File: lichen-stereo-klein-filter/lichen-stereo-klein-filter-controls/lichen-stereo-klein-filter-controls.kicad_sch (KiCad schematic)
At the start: 39 parts, among them J1 Thonkiconn_Mono_Audio_Jack, J2 Thonkiconn_Mono_Audio_Jack, J3 Thonkiconn_Mono_Audio_Jack, J4 Thonkiconn_Mono_Audio_Jack, J5 Thonkiconn_Mono_Audio_Jack, J6 Thonkiconn_Mono_Audio_Jack, J7 Conn_02x07_Top_Bottom, U1 TL074

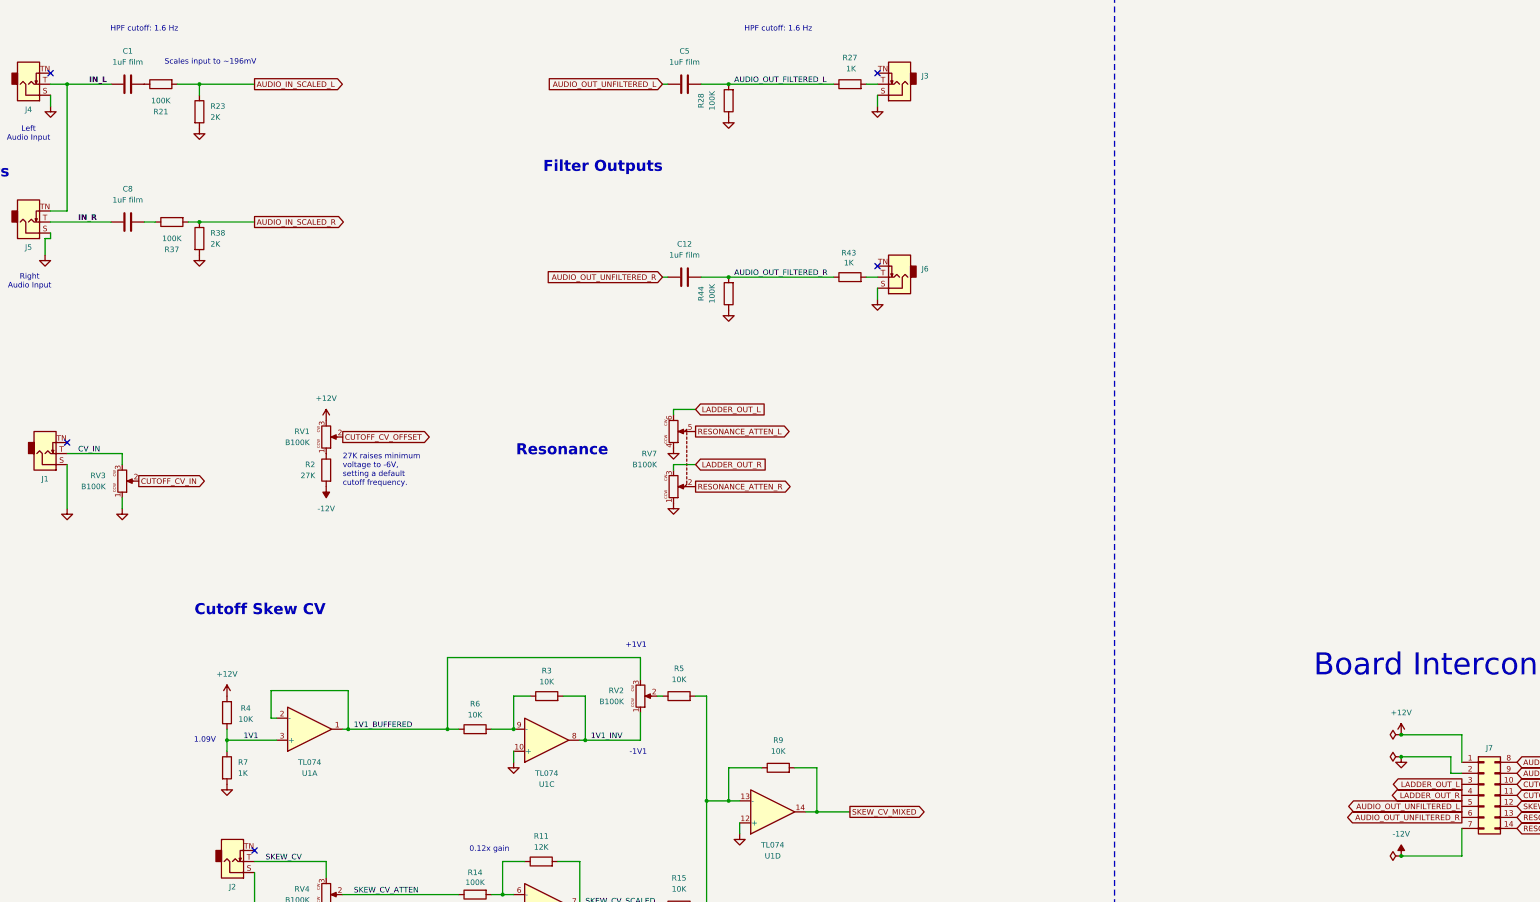
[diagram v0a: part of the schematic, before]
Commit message: feat: Updates Crustose, Cladonia and YouMe Transformer. Adds Stereo Latencies.
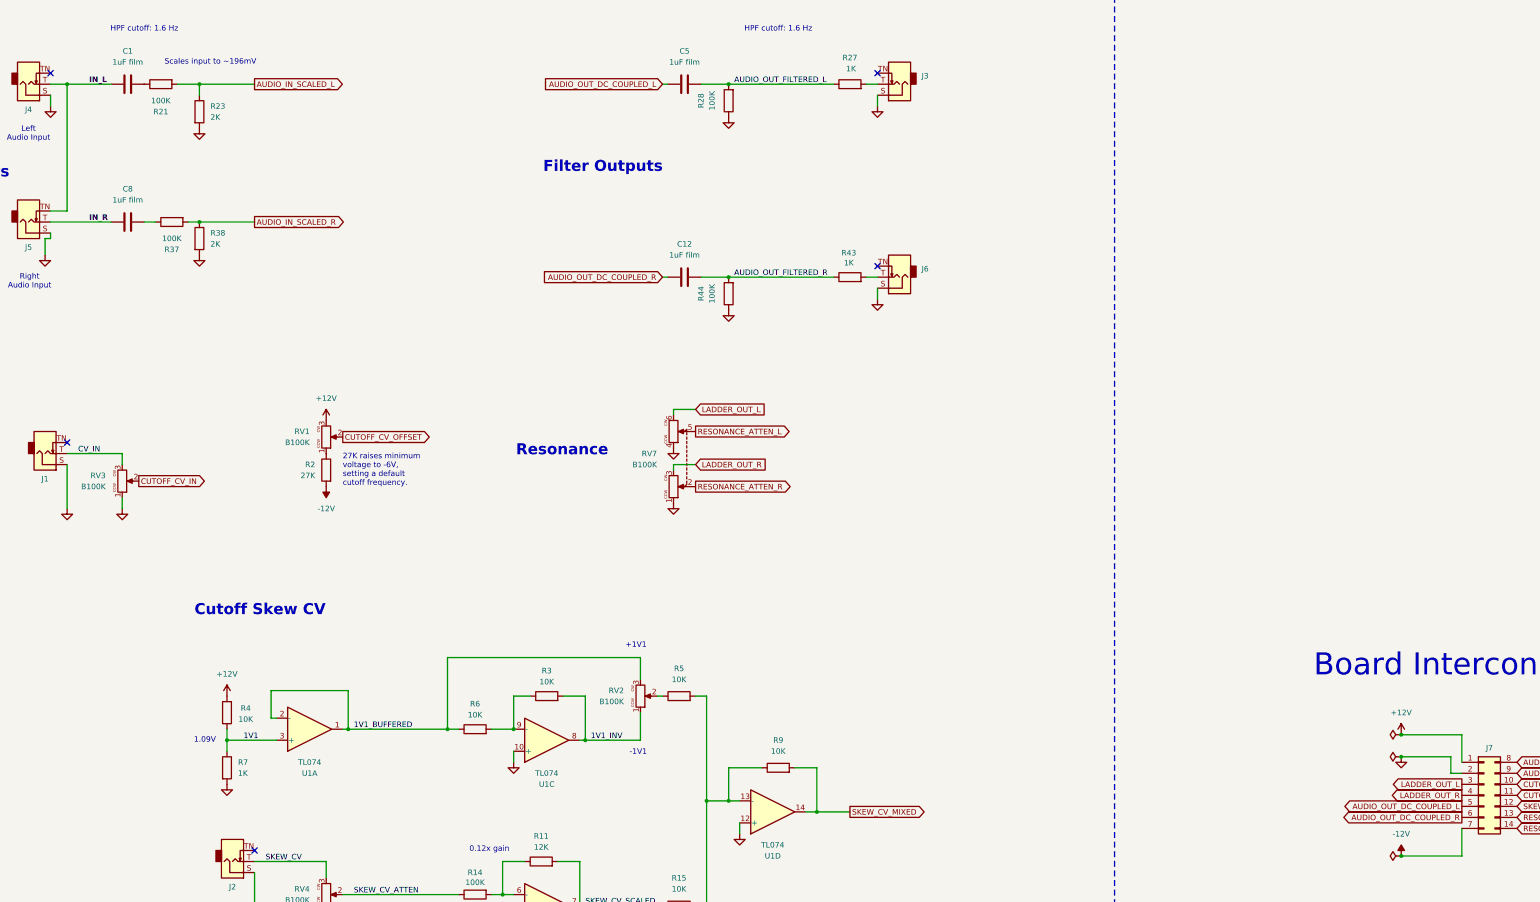
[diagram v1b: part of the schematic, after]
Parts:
- J3, J6: footprint Lichen:Audio_Jack_Thonkiconn_Mono -> Lichen:Audio_Jack_Thonkiconn_Mono_Right_Overhang
- J4, J5: footprint Lichen:Audio_Jack_Thonkiconn_Mono -> Lichen:Audio_Jack_Thonkiconn_Mono_Left_Overhang
- J7: value Conn_02x07_Top_Bottom -> 02x07 Socket; LCSC (none) -> C84005; Manufacturer (none) -> BOOMELE(Boom Precision Elec); Part Number (none) -> 2.54-2*7PFemale Headers
- R11: JLCPCB ID C22790 -> (none); LCSC (none) -> C22790
- R15, R3, R6, R9: JLCPCB ID C25804 -> (none); LCSC (none) -> C25804
- R4, R5: LCSC (none) -> C25804
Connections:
- net AUDIO_OUT_UNFILTERED_L renamed AUDIO_OUT_DC_COUPLED_L
- net AUDIO_OUT_UNFILTERED_R renamed AUDIO_OUT_DC_COUPLED_R
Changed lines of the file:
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@@
 	)
 	(label "IN_R"
-		(at 71.12 80.01 0)
+		(at 73.66 80.01 0)
 		(effects
 			(font
@@
 		)
 	)
-	(global_label "AUDIO_OUT_UNFILTERED_R"
+	(global_label "AUDIO_OUT_DC_COUPLED_R"
 		(shape output)
 		(at 389.89 217.17 180)
@@
 		)
 		(property "Intersheetrefs" "${INTERSHEET_REFS}"
-			(at 362.2909 217.17 0)
+			(at 361.3233 217.17 0)
 			(effects
 				(font
@@
 		)
 	)
-	(global_label "AUDIO_OUT_UNFILTERED_L"
+	(global_label "AUDIO_OUT_DC_COUPLED_L"
 		(shape output)
 		(at 389.89 214.63 180)
@@
 		)
 		(property "Intersheetrefs" "${INTERSHEET_REFS}"
-			(at 362.5328 214.63 0)
+			(at 361.5652 214.63 0)
 			(effects
 				(font
@@
 		)
 	)
-	(global_label "AUDIO_OUT_UNFILTERED_L"
+	(global_label "AUDIO_OUT_DC_COUPLED_L"
 		(shape input)
 		(at 205.74 48.26 180)
@@
 		)
 		(property "Intersheetrefs" "${INTERSHEET_REFS}"
-			(at 178.3828 48.26 0)
+			(at 177.4152 48.26 0)
 			(effects
 				(font
@@
 		)
 	)
-	(global_label "AUDIO_OUT_UNFILTERED_R"
+	(global_label "AUDIO_OUT_DC_COUPLED_R"
 		(shape input)
 		(at 205.74 92.71 180)
@@
 		)
 		(property "Intersheetrefs" "${INTERSHEET_REFS}"
-			(at 178.1409 92.71 0)
+			(at 177.1733 92.71 0)
 			(effects
 				(font
@@
 			)
 		)
-		(property "Datasheet" "https://jlcpcb.com/api/file/downloadByFileSystemAccessId/8579706381320323072"
+		(property "Datasheet" "https://www.lcsc.com/datasheet/lcsc_datasheet_2206010045_UNI-ROYAL-Uniroyal-Elec-0603WAF1002T5E_C25804.pdf"
 			(at 105.41 193.04 0)
 			(effects
@@
 			)
 		)
+		(property "LCSC" "C25804"
+			(at 104.14 177.8 0)
+			(effects
+				(font
+					(size 1.27 1.27)
+				)
+				(hide yes)
+			)
+		)
 		(pin "1"
 		)
@@
 			)
 		)
-		(property "Footprint" "Lichen:Audio_Jack_Thonkiconn_Mono"
+		(property "Footprint" "Lichen:Audio_Jack_Thonkiconn_Mono_Left_Overhang"
 			(at 60.706 32.512 0)
 			(effects
@@
 			)
 		)
-		(property "Footprint" "Lichen:Audio_Jack_Thonkiconn_Mono"
+		(property "Footprint" "Lichen:Audio_Jack_Thonkiconn_Mono_Right_Overhang"
 			(at 259.334 32.512 0)
 			(effects
@@
 		)
 		(instances
-			(project ""
+			(project "lichen-stereo-klein-filter-controls"
 				(path "/bf38fd3d-174f-4d81-a157-162ed62e96ed"
 					(reference "H2")
@@
 			)
 		)
-		(property "Datasheet" "https://jlcpcb.com/api/file/downloadByFileSystemAccessId/8579706381320323072"
+		(property "Datasheet" "https://www.lcsc.com/datasheet/lcsc_datasheet_2206010045_UNI-ROYAL-Uniroyal-Elec-0603WAF1002T5E_C25804.pdf"
 			(at 209.55 189.23 0)
 			(effects
@@
 			)
 		)
+		(property "LCSC" "C25804"
+			(at 224.79 187.96 0)
+			(effects
+				(font
+					(size 1.27 1.27)
+				)
+				(hide yes)
+			)
+		)
 		(pin "1"
 		)
@@
 		)
 		(instances
-			(project ""
+			(project "lichen-stereo-klein-filter-controls"
 				(path "/bf38fd3d-174f-4d81-a157-162ed62e96ed"
 					(reference "H1")
@@
 			)
 		)
-		(property "Datasheet" "https://jlcpcb.com/api/file/downloadByFileSystemAccessId/8579706381320323072"
+		(property "Datasheet" "https://www.lcsc.com/datasheet/lcsc_datasheet_2206010045_UNI-ROYAL-Uniroyal-Elec-0603WAF1002T5E_C25804.pdf"
 			(at 232.41 205.74 0)
 			(effects
@@
 			)
 		)
-		(property "JLCPCB ID" "C25804"
+		(property "LCSC" "C25804"
 			(at 247.65 204.47 0)
 			(effects
@@
 			)
 		)
-		(property "Footprint" "Lichen:Audio_Jack_Thonkiconn_Mono"
+		(property "Footprint" "Lichen:Audio_Jack_Thonkiconn_Mono_Right_Overhang"
 			(at 259.334 76.962 0)
 			(effects
@@
 			)
 		)
-		(property "Footprint" "Lichen:Audio_Jack_Thonkiconn_Mono"
+		(property "Footprint" "Lichen:Audio_Jack_Thonkiconn_Mono_Left_Overhang"
 			(at 60.706 64.262 0)
 			(effects
@@
 			)
 		)
-		(property "Datasheet" "https://jlcpcb.com/api/file/downloadByFileSystemAccessId/8579706381320323072"
+		(property "Datasheet" "https://www.lcsc.com/datasheet/lcsc_datasheet_2206010045_UNI-ROYAL-Uniroyal-Elec-0603WAF1002T5E_C25804.pdf"
 			(at 209.55 237.49 0)
 			(effects
@@
 			)
 		)
-		(property "JLCPCB ID" "C25804"
+		(property "LCSC" "C25804"
 			(at 224.79 236.22 0)
 			(effects
@@
 			)
 		)
-		(property "Datasheet" "https://jlcpcb.com/api/file/downloadByFileSystemAccessId/8579706381320323072"
+		(property "Datasheet" "https://www.lcsc.com/datasheet/lcsc_datasheet_2206010045_UNI-ROYAL-Uniroyal-Elec-0603WAF1002T5E_C25804.pdf"
 			(at 179.07 189.23 0)
 			(effects
@@
 			)
 		)
-		(property "JLCPCB ID" "C25804"
+		(property "LCSC" "C25804"
 			(at 194.31 187.96 0)
 			(effects
@@
 			)
 		)
-		(property "Datasheet" "https://jlcpcb.com/api/file/downloadByFileSystemAccessId/8579706381320323072"
+		(property "Datasheet" "https://www.lcsc.com/datasheet/lcsc_datasheet_2206010045_UNI-ROYAL-Uniroyal-Elec-0603WAF1002T5E_C25804.pdf"
 			(at 162.56 196.85 0)
 			(effects
@@
 			)
 		)
-		(property "JLCPCB ID" "C25804"
+		(property "LCSC" "C25804"
 			(at 177.8 195.58 0)
 			(effects
@@
 			)
 		)
-		(property "Value" "Conn_02x07_Top_Bottom"
+		(property "Value" "02x07 Socket"
 			(at 396.24 200.66 0)
 			(effects
@@
 			)
 		)
-		(property "Datasheet" "~"
+		(property "Datasheet" "https://www.lcsc.com/datasheet/lcsc_datasheet_2304140030_BOOMELE-Boom-Precision-Elec-2-54-2-7P_C84005.pdf"
+			(at 394.97 212.09 0)
+			(effects
+				(font
+					(size 1.27 1.27)
+				)
+				(hide yes)
+			)
+		)
+		(property "Description" "4P 2 2.54mm 2.54mm 2.5A 2x7P 8.5mm Brass Gold Square Hole Surface Mount,Vertical Top SMD,P=2.54mm Female Headers"
+			(at 394.97 212.09 0)
+			(effects
+				(font
+					(size 1.27 1.27)
+				)
+				(hide yes)
+			)
+		)
+		(property "Manufacturer" "BOOMELE(Boom Precision Elec)"
+			(at 394.97 212.09 0)
+			(effects
+				(font
+					(size 1.27 1.27)
+				)
+				(hide yes)
+			)
+		)
+		(property "Part Number" "2.54-2*7PFemale Headers"
 			(at 394.97 212.09 0)
 			(effects
@@
 			)
 		)
-		(property "Description" "Generic connector, double row, 02x07, top/bottom pin numbering scheme (row 1: 1...pins_per_row, row2: pins_per_row+1 ... num_pins), script generated (kicad-library-utils/schlib/autogen/connector/)"
+		(property "LCSC" "C84005"
 			(at 394.97 212.09 0)
 			(effects
@@
 			)
 		)
-		(property "JLCPCB ID" "C22790"
+		(property "LCSC" "C22790"
 			(at 193.04 226.06 0)
 			(effects
